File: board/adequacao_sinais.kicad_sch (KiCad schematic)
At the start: 2 parts, among them U5 LM324

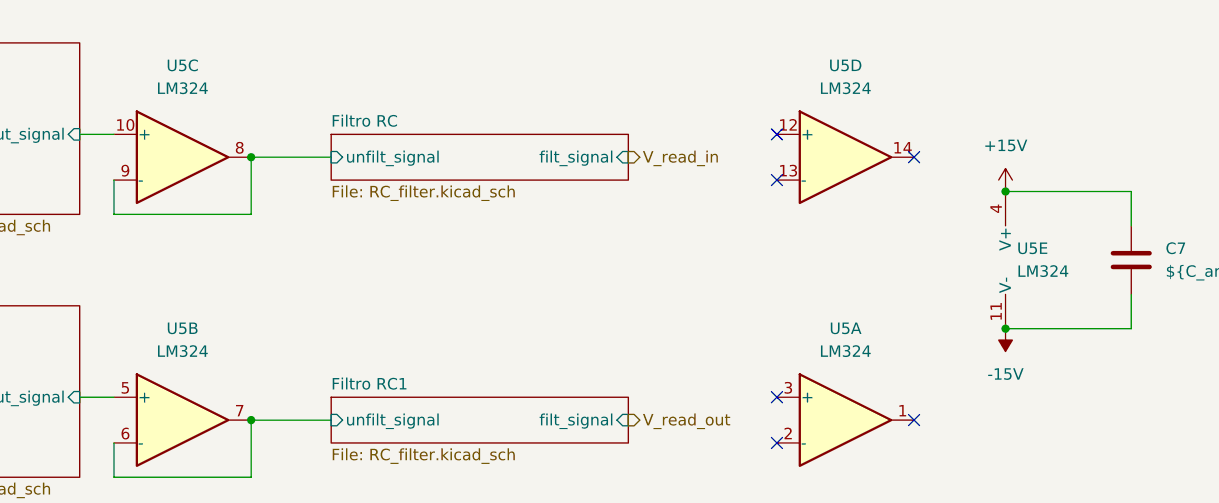
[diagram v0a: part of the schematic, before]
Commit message: Finalização da placa, trilhas, planos de terra e footprint TJA1050
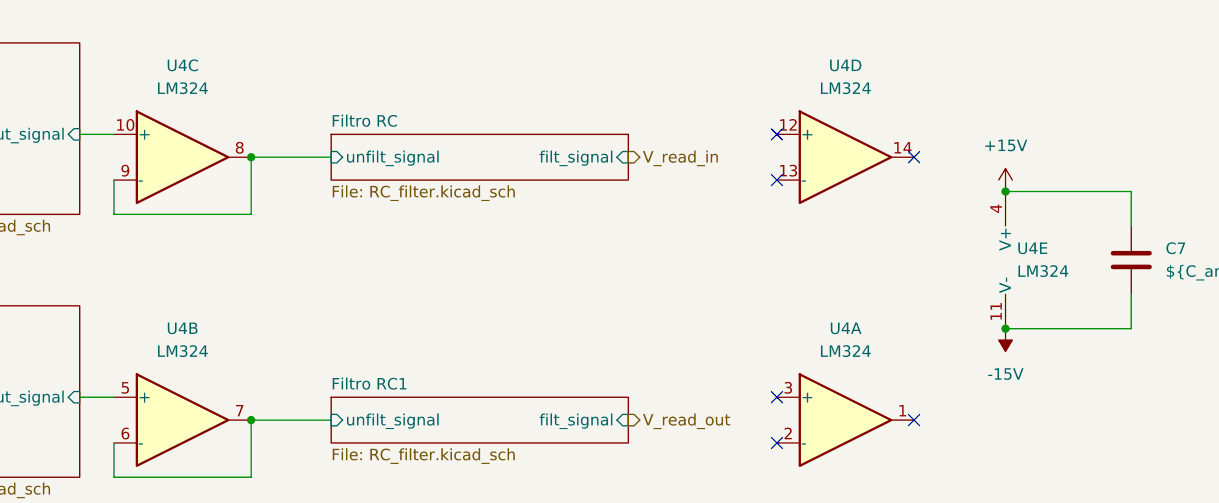
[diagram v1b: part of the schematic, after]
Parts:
- renumbered U5 to U4
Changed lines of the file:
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@@
 		(dnp no)
 		(fields_autoplaced yes)
-		(property "Reference" "U5"
+		(property "Reference" "U4"
 			(at 166.37 24.13 0)
 			(effects
@@
 			(project "board"
 				(path "/d7be55ed-3561-4de6-aa99-76e883d44fb9/484b45ac-854b-4808-a94a-82052b89ba4d"
-					(reference "U5")
+					(reference "U4")
 					(unit 4)
 				)
@@
 		(dnp no)
 		(fields_autoplaced yes)
-		(property "Reference" "U5"
+		(property "Reference" "U4"
 			(at 185.42 44.4499 0)
 			(effects
@@
 			(project "board"
 				(path "/d7be55ed-3561-4de6-aa99-76e883d44fb9/484b45ac-854b-4808-a94a-82052b89ba4d"
-					(reference "U5")
+					(reference "U4")
 					(unit 5)
 				)
@@
 		(dnp no)
 		(fields_autoplaced yes)
-		(property "Reference" "#PWR38"
+		(property "Reference" "#PWR35"
 			(at 184.15 49.53 0)
 			(effects
@@
 			(project "board"
 				(path "/d7be55ed-3561-4de6-aa99-76e883d44fb9/484b45ac-854b-4808-a94a-82052b89ba4d"
-					(reference "#PWR38")
+					(reference "#PWR35")
 					(unit 1)
 				)
@@
 		(dnp no)
 		(fields_autoplaced yes)
-		(property "Reference" "U5"
+		(property "Reference" "U4"
 			(at 92.71 24.13 0)
 			(effects
@@
 			(project "board"
 				(path "/d7be55ed-3561-4de6-aa99-76e883d44fb9/484b45ac-854b-4808-a94a-82052b89ba4d"
-					(reference "U5")
+					(reference "U4")
 					(unit 3)
 				)
@@
 		(dnp no)
 		(fields_autoplaced yes)
-		(property "Reference" "#PWR37"
+		(property "Reference" "#PWR34"
 			(at 184.15 41.91 0)
 			(effects
@@
 			(project "board"
 				(path "/d7be55ed-3561-4de6-aa99-76e883d44fb9/484b45ac-854b-4808-a94a-82052b89ba4d"
-					(reference "#PWR37")
+					(reference "#PWR34")
 					(unit 1)
 				)
@@
 		(dnp no)
 		(fields_autoplaced yes)
-		(property "Reference" "U5"
+		(property "Reference" "U4"
 			(at 166.37 53.34 0)
 			(effects
@@
 			(project "board"
 				(path "/d7be55ed-3561-4de6-aa99-76e883d44fb9/484b45ac-854b-4808-a94a-82052b89ba4d"
-					(reference "U5")
+					(reference "U4")
 					(unit 1)
 				)
@@
 		(dnp no)
 		(fields_autoplaced yes)
-		(property "Reference" "U5"
+		(property "Reference" "U4"
 			(at 92.71 53.34 0)
 			(effects
@@
 			(project "board"
 				(path "/d7be55ed-3561-4de6-aa99-76e883d44fb9/484b45ac-854b-4808-a94a-82052b89ba4d"
-					(reference "U5")
+					(reference "U4")
 					(unit 2)
 				)

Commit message: Criação da placa de alimentação
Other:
- company: (none) -> Escola Politécnica da Universidade de São Paulo
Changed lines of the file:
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@@
 	(generator_version "8.0")
 	(paper "A4")
+	(title_block
+		(date "2025-10-02")
+		(company "Escola Politécnica da Universidade de São Paulo")
+	)
 	(junction
 		(at 100.33 63.5)
@@
 			(project "board"
 				(path "/d7be55ed-3561-4de6-aa99-76e883d44fb9/484b45ac-854b-4808-a94a-82052b89ba4d"
-					(page "13")
+					(page "12")
 				)
 			)
@@
 			(project "board"
 				(path "/d7be55ed-3561-4de6-aa99-76e883d44fb9/484b45ac-854b-4808-a94a-82052b89ba4d"
-					(page "15")
+					(page "13")
 				)
 			)
@@
 			(project "board"
 				(path "/d7be55ed-3561-4de6-aa99-76e883d44fb9/484b45ac-854b-4808-a94a-82052b89ba4d"
-					(page "6")
+					(page "15")
 				)
 			)
@@
 			(project "board"
 				(path "/d7be55ed-3561-4de6-aa99-76e883d44fb9/484b45ac-854b-4808-a94a-82052b89ba4d"
-					(page "2")
+					(page "10")
 				)
 			)
@@
 			(project "board"
 				(path "/d7be55ed-3561-4de6-aa99-76e883d44fb9/484b45ac-854b-4808-a94a-82052b89ba4d"
-					(page "12")
+					(page "18")
 				)
 			)
@@
 			(project "board"
 				(path "/d7be55ed-3561-4de6-aa99-76e883d44fb9/484b45ac-854b-4808-a94a-82052b89ba4d"
-					(page "14")
+					(page "19")
 				)
 			)
@@
 			(project "board"
 				(path "/d7be55ed-3561-4de6-aa99-76e883d44fb9/484b45ac-854b-4808-a94a-82052b89ba4d"
-					(page "8")
+					(page "14")
 				)
 			)
@@
 			(project "board"
 				(path "/d7be55ed-3561-4de6-aa99-76e883d44fb9/484b45ac-854b-4808-a94a-82052b89ba4d"
-					(page "4")
+					(page "9")
 				)
 			)
@@
 			(project "board"
 				(path "/d7be55ed-3561-4de6-aa99-76e883d44fb9/484b45ac-854b-4808-a94a-82052b89ba4d"
-					(page "7")
+					(page "16")
 				)
 			)
@@
 			(project "board"
 				(path "/d7be55ed-3561-4de6-aa99-76e883d44fb9/484b45ac-854b-4808-a94a-82052b89ba4d"
-					(page "10")
+					(page "17")
 				)
 			)
@@
 			(project "board"
 				(path "/d7be55ed-3561-4de6-aa99-76e883d44fb9/484b45ac-854b-4808-a94a-82052b89ba4d"
-					(page "5")
-				)
-			)
+					(page "8")
+				)
+			)
